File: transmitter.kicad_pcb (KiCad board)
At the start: 6 copper layers, 200 x 110 mm, 246 parts, among them IC1 W9864G6KH-6, IC2 TPS61165DBVR, IC3 MT25QL128ABA1ESE-0SIT, IC4 USBLC6-2SC6, J1 AFC01-S40FCA-00, J2 AFC07-S10ECC-00, J3 B2B-PH-K-S, J4 B2B-PH-K-S, J5 B3B-PH-K-S, J6 USB4085-GF-A, J7 Conn_01x05, J9 Conn_02x06_Odd_Even, Q1 AO3400A, Q2 AO3400A, Q3 SI2301CDS-T1-GE3, Q4 AO3400A, SW1 Button SPST SMD Tactile Switch, SW2 Button SPST SMD Tactile Switch, SW3 Button SPST SMD Tactile Switch, SW4 Button SPST SMD Tactile Switch, SW5 Button SPST SMD Tactile Switch, SW6 Button SPST SMD Tactile Switch, SW7 SW_SPDT_MSM, SW8 Button SPST SMD Tactile Switch, SW9 RotaryEncoder_Switch, U1 STM32H743ZIT6TR, U2 CAT24C256, U3 MP2667GG-0000-Z, U4 AMS1117-3.3, U5 TPS61252DSG, U6 PCA9554APW, Y1 32.768KHZ, Y2 X322525MOB4SI-25MHz

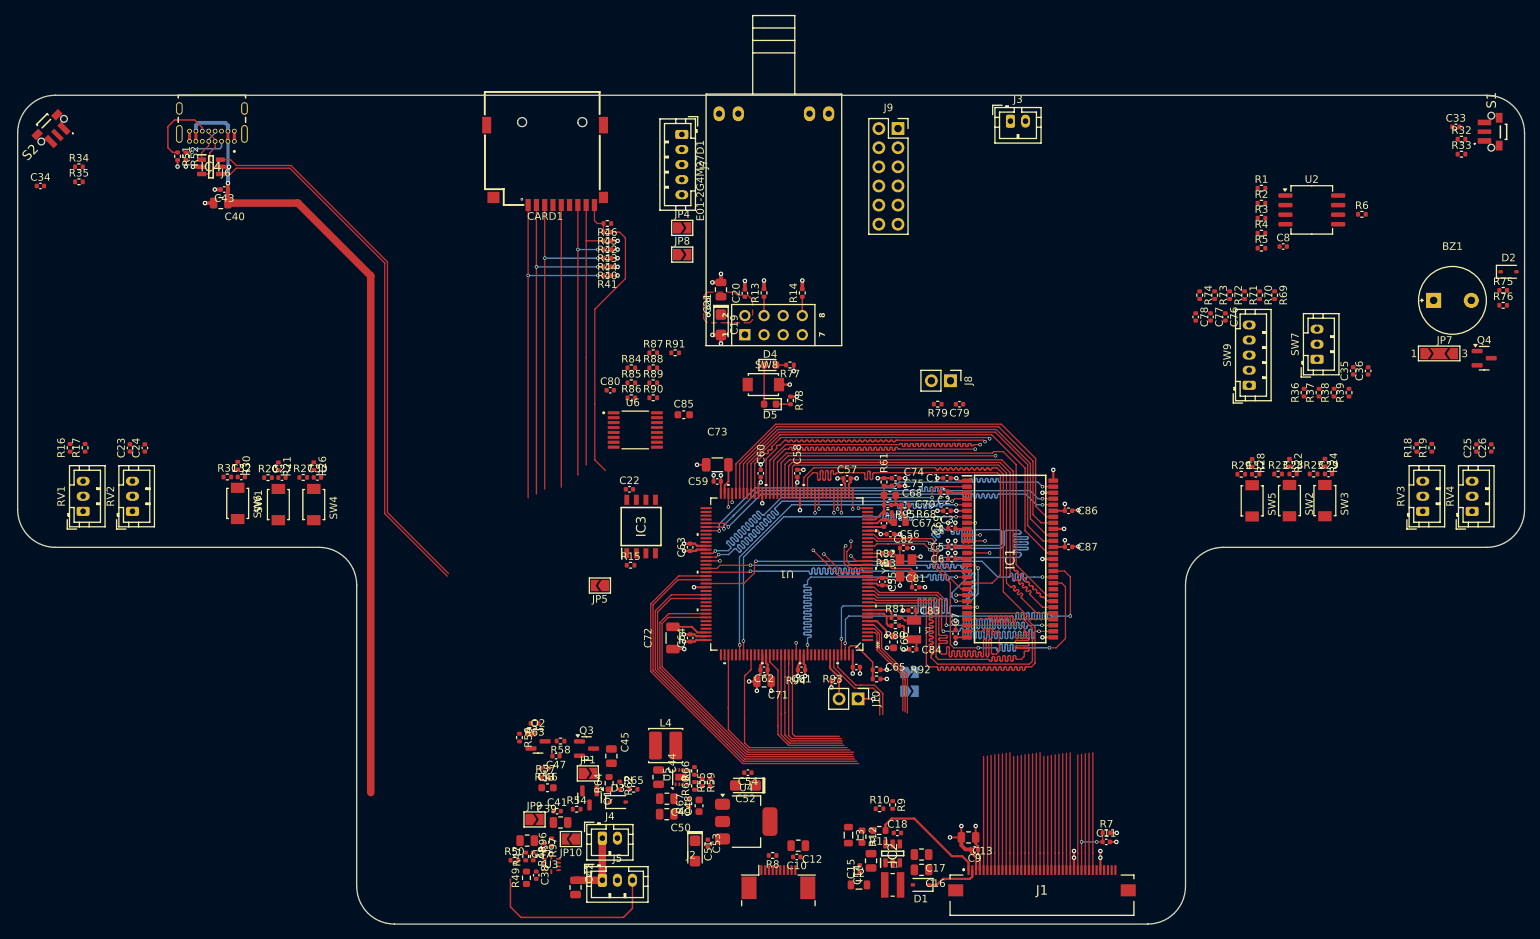
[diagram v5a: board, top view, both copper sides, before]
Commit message: mala zmiana niektorych polaczen i layoutu, podlaczenie usb, rozpoczecie routowania sekcji zasilania - charger ic
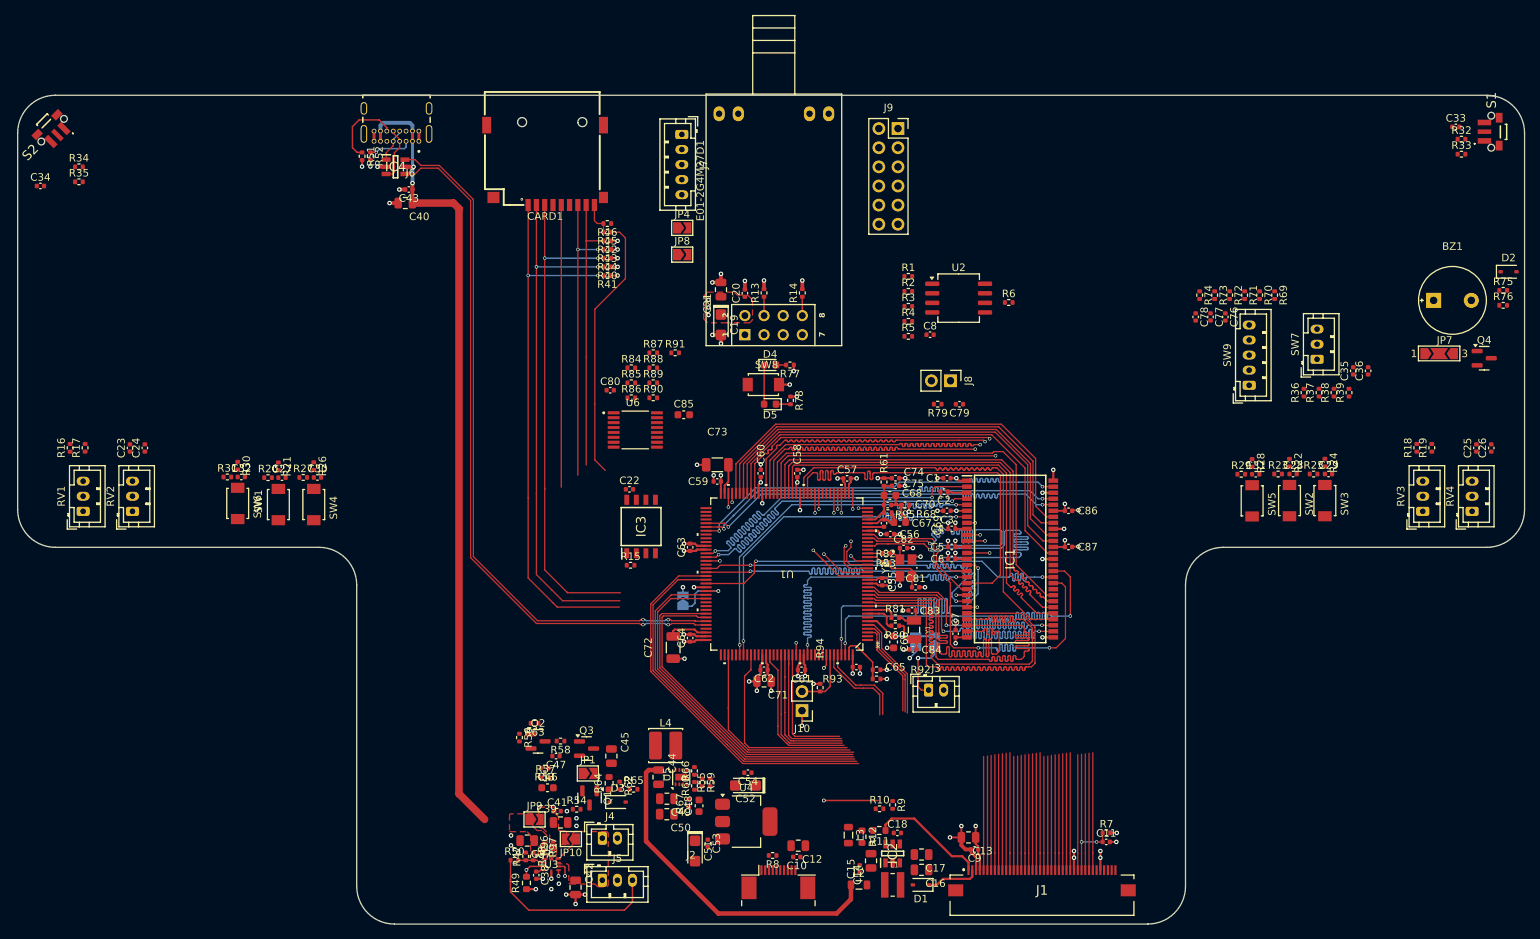
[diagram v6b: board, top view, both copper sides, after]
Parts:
- JP5: moved to B.Cu
- moved J3 76.3 mm to (142.4, 100.5)
- moved C8 48.3 mm to (142.6, 53.3)
- moved R1 48.3 mm to (139.7, 45.5)
- moved R2 48.3 mm to (139.7, 47.5)
- moved R3 48.3 mm to (139.7, 49.5)
- moved R4 48.3 mm to (139.7, 51.5)
- moved R5 48.3 mm to (139.7, 53.5)
- moved R6 48.3 mm to (153.0, 49.0)
- moved U2 48.3 mm to (146.4, 48.4)
- moved J6 24.5 mm to (71.8, 23.2)
- moved C40 24.5 mm to (73.0, 35.8)
- moved C43 24.5 mm to (73.4, 34.0)
- moved R51 24.5 mm to (67.2, 29.6)
- moved IC4 24.5 mm to (71.6, 31.0)
- moved R52 24.5 mm to (68.3, 29.6)
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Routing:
- net VSYS_SW: track 0.00 -> 44.8 mm
- net /Project Architecture/LCD - Backlight/BACKLIGHT_PWM: track 0.00 -> 26.7 mm, vias 0 -> 2
- net /Project Architecture/MCU - IO/SDMMC2_D2: track 48.9 -> 73.2 mm
- net /Project Architecture/MCU - IO/SDMMC2_D3: track 47.3 -> 70.6 mm
- net /Project Architecture/MCU - IO/SDMMC2_CMD: track 45.5 -> 67.7 mm
- net /Project Architecture/Interface - USB FS/USB_OTG_FS_DP: track 72.3 -> 93.4 mm, vias 0 -> 2
- net /Project Architecture/Interface - USB FS/USB_OTG_FS_DN: track 72.5 -> 93.3 mm, vias 0 -> 2
- net +BATT: track 9.14 -> 0.00 mm
- net /Project Architecture/LCD - Connectors/LTDC_R6: track 52.4 -> 43.2 mm
- net Net-(J3-Pin_1): track 0.00 -> 8.74 mm, vias 0 -> 1
- net /Project Architecture/LCD - Connectors/LTDC_R3: track 51.7 -> 43.0 mm
- net /Project Architecture/LCD - Connectors/LTDC_G2: track 50.5 -> 42.2 mm
- net /Project Architecture/LCD - Connectors/LTDC_R4: track 50.4 -> 42.3 mm
- net Net-(JP5-A): track 0.00 -> 7.88 mm, vias 0 -> 1
- net /Project Architecture/LCD - Connectors/LTDC_VSYNC: track 51.0 -> 43.2 mm
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- added copper zone on F.Cu, net +BATT
- added copper zone on F.Cu, net Net-(U3-IN)
- added copper zone on F.Cu, net Net-(U3-SYS)
- added copper zone on F.Cu, net VBUS
- added copper zone on F.Cu, net VSYS
